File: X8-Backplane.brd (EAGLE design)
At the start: 101.9 x 101.6 mm, 17 parts

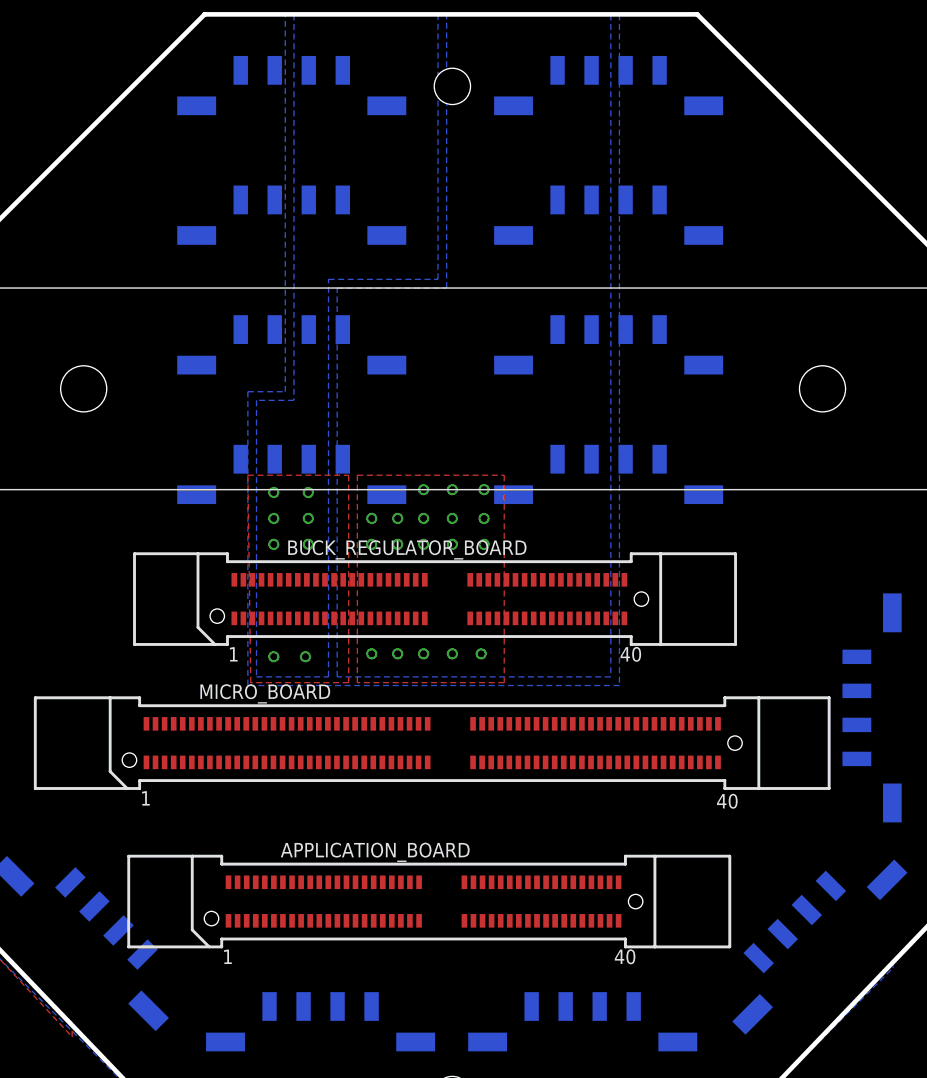
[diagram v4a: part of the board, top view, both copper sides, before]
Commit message: Routed connections from micro board
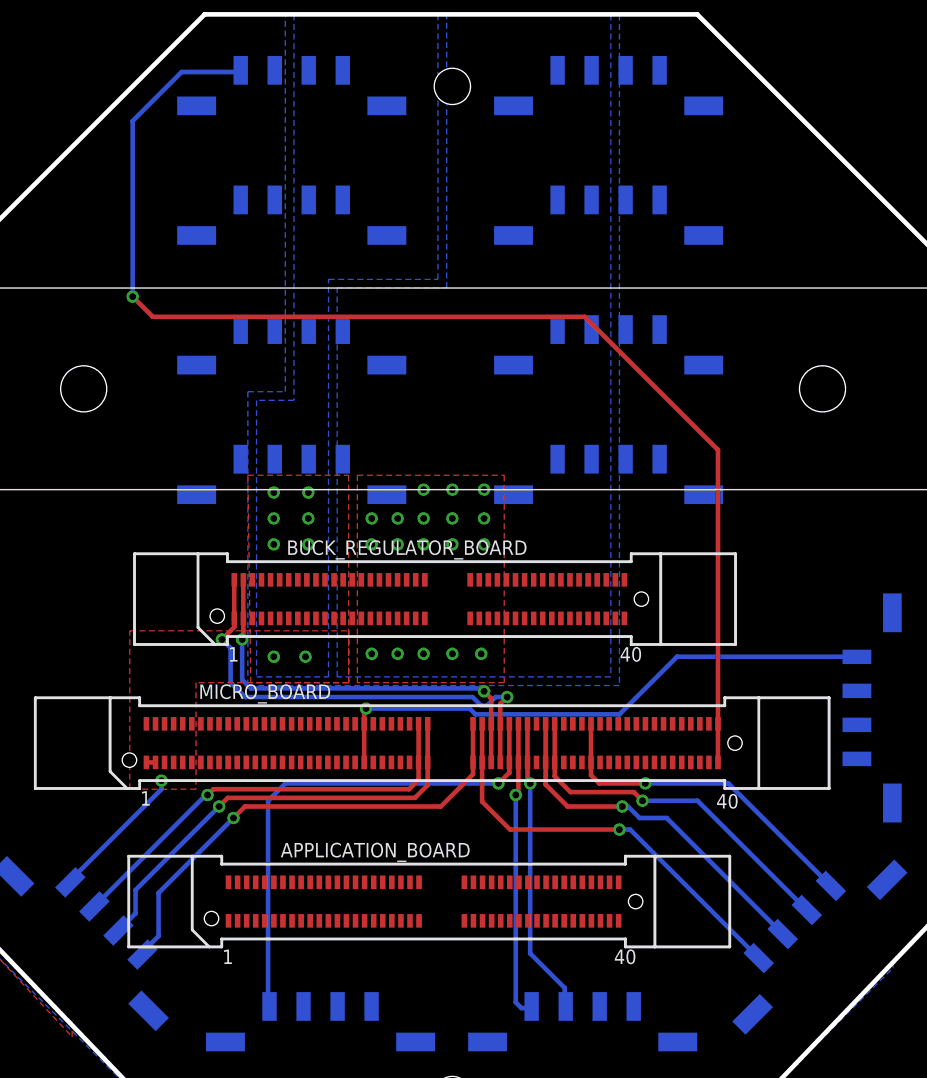
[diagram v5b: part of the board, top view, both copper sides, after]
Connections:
- removed net N$7: TEMP_SENSOR.C1
- removed net SCL: NAV_COM.C4
- removed net SDA: NAV_COM.C3
- new net BACK_UP_TEMP_DATA: MICRO_BOARD.49, MICRO_BOARD.50, TEMP_SENSOR.C1
- new net NAV_SCL: MICRO_BOARD.83, MICRO_BOARD.84, NAV_COM.C2
- new net NAV_SDA: MICRO_BOARD.81, MICRO_BOARD.82, NAV_COM.C3
- net +5V: now also MICRO_BOARD.1, MICRO_BOARD.10, MICRO_BOARD.11, MICRO_BOARD.12, MICRO_BOARD.2, MICRO_BOARD.3, MICRO_BOARD.4, MICRO_BOARD.5, MICRO_BOARD.6, MICRO_BOARD.7, MICRO_BOARD.8, MICRO_BOARD.9, SOLENOID_DATA.C4; no longer SOLENOID_DATA.C1
- net BUCK_SCL: now also MICRO_BOARD.71, MICRO_BOARD.72
- net BUCK_SDA: now also MICRO_BOARD.69, MICRO_BOARD.70
- net CANH: now also BRICKS_COM.C3, MICRO_BOARD.77, MICRO_BOARD.78; no longer BRICKS_COM.C4
- net CANL: now also BRICKS_COM.C4, MICRO_BOARD.75, MICRO_BOARD.76; no longer BRICKS_COM.C3
- net CLK: now also MICRO_BOARD.63, MICRO_BOARD.64, SOLENOID_DATA.C2; no longer SOLENOID_DATA.C3
- net DATA: now also MICRO_BOARD.65, MICRO_BOARD.66, SOLENOID_DATA.C1; no longer SOLENOID_DATA.C4
- net ENABLE: now also MICRO_BOARD.61, MICRO_BOARD.62, SOLENOID_DATA.C3; no longer SOLENOID_DATA.C2
- net GND: now also MICRO_BOARD.21, MICRO_BOARD.22, MICRO_BOARD.23, MICRO_BOARD.24, MICRO_BOARD.25, MICRO_BOARD.26, MICRO_BOARD.27, MICRO_BOARD.28, MICRO_BOARD.29, MICRO_BOARD.30, MICRO_BOARD.31, MICRO_BOARD.32, MICRO_BOARD.33, MICRO_BOARD.34, MICRO_BOARD.35, MICRO_BOARD.36
- net MAIN_SERVO: now also MICRO_BOARD.73, MICRO_BOARD.74
- net SECOND_SERVO: now also MICRO_BOARD.119, MICRO_BOARD.120
- net SONAR_DAC: now also MICRO_BOARD.91, MICRO_BOARD.92
- net SONAR_PWM: now also MICRO_BOARD.67, MICRO_BOARD.68, NAV_COM.C4; no longer NAV_COM.C2
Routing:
- net SECOND_SERVO: track 0.00 -> 111.6 mm, vias 0 -> 1
- net BACK_UP_TEMP_DATA: track 0.00 -> 50.4 mm, vias 0 -> 1
- net MAIN_SERVO: track 0.00 -> 44.8 mm, vias 0 -> 1
- net DATA: track 0.00 -> 42.5 mm, vias 0 -> 1
- net BUCK_SCL: track 0.00 -> 41.4 mm, vias 0 -> 2
- net CLK: track 0.00 -> 39.2 mm, vias 0 -> 1
- net ENABLE: track 0.00 -> 38.1 mm, vias 0 -> 1
- net BUCK_SDA: track 0.00 -> 37.1 mm, vias 0 -> 2
- net SONAR_PWM: track 0.00 -> 37.0 mm, vias 0 -> 1
- net NAV_SCL: track 0.00 -> 31.7 mm, vias 0 -> 1
- net NAV_SDA: track 0.00 -> 31.7 mm, vias 0 -> 1
- net SONAR_DAC: track 0.00 -> 29.7 mm, vias 0 -> 1
- net CANL: track 0.00 -> 26.3 mm, vias 0 -> 1
- net CANH: track 0.00 -> 26.3 mm, vias 0 -> 1
- net +5V: track 0.00 -> 13.1 mm, vias 8 -> 9

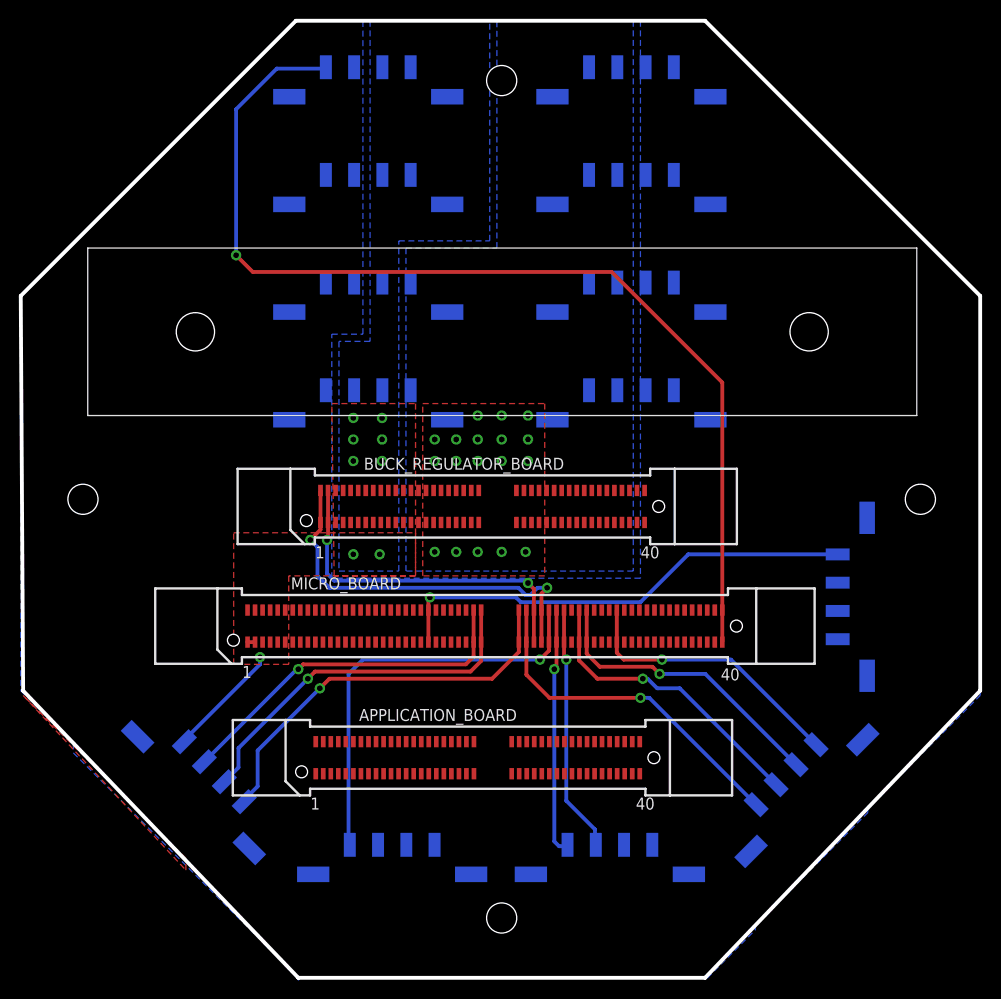
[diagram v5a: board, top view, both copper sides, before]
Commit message: Changed around the order of the connectors
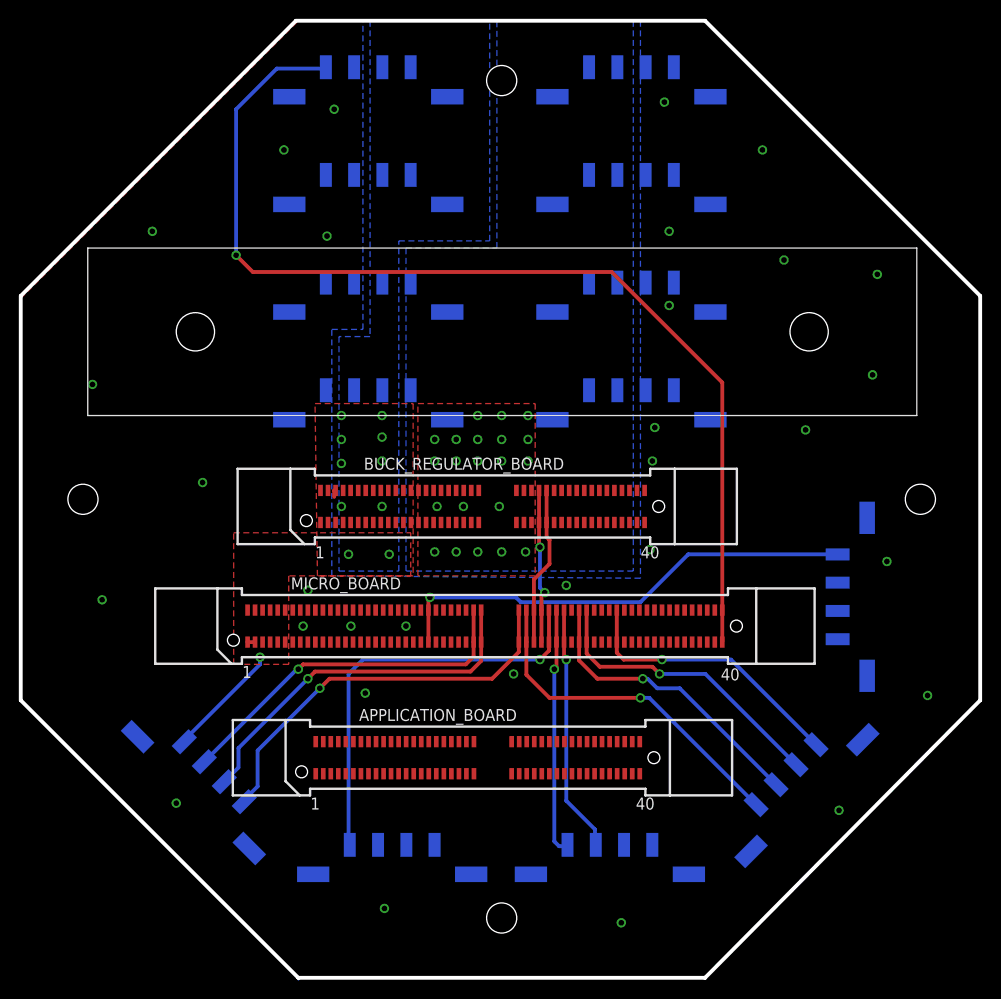
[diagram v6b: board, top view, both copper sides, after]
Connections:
- net +12V: now also BUCK_REGULATOR_BOARD.27, BUCK_REGULATOR_BOARD.28, BUCK_REGULATOR_BOARD.29, BUCK_REGULATOR_BOARD.30; no longer BUCK_REGULATOR_BOARD.51, BUCK_REGULATOR_BOARD.52
- net +5V: now also BUCK_REGULATOR_BOARD.1, BUCK_REGULATOR_BOARD.2, BUCK_REGULATOR_BOARD.3, BUCK_REGULATOR_BOARD.4
- net BUCK_SCL: now also BUCK_REGULATOR_BOARD.51, BUCK_REGULATOR_BOARD.52; no longer BUCK_REGULATOR_BOARD.1, BUCK_REGULATOR_BOARD.2
- net BUCK_SDA: now also BUCK_REGULATOR_BOARD.53, BUCK_REGULATOR_BOARD.54; no longer BUCK_REGULATOR_BOARD.3, BUCK_REGULATOR_BOARD.4
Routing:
- net BUCK_SCL: track 41.4 -> 16.5 mm
- net BUCK_SDA: track 37.1 -> 16.9 mm, vias 2 -> 0
- net +5V: track 13.1 -> 13.9 mm, vias 9 -> 11
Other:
- outline, holes or cut-outs redrawn

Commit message: Changed more connector lines
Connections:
- net BUCK_SCL: now also BUCK_REGULATOR_BOARD.53, BUCK_REGULATOR_BOARD.54; no longer BUCK_REGULATOR_BOARD.51, BUCK_REGULATOR_BOARD.52
- net BUCK_SDA: now also BUCK_REGULATOR_BOARD.51, BUCK_REGULATOR_BOARD.52; no longer BUCK_REGULATOR_BOARD.53, BUCK_REGULATOR_BOARD.54
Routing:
- net BUCK_SDA: track 16.9 -> 16.3 mm
- net BUCK_SCL: track 16.5 -> 16.4 mm, vias 2 -> 0
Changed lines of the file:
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@@
 <contactref element="MICRO_BOARD" pad="71"/>
 <wire x1="52.736" y1="37.768" x2="52.736" y2="34.368" width="0.4064" layer="1"/>
-<contactref element="BUCK_REGULATOR_BOARD" pad="52"/>
-<contactref element="BUCK_REGULATOR_BOARD" pad="51"/>
-<wire x1="52.482" y1="50.468" x2="52.482" y2="47.068" width="0.4064" layer="1"/>
-<wire x1="52.482" y1="47.068" x2="52.482" y2="44.546" width="0.4064" layer="1"/>
-<wire x1="52.482" y1="44.546" x2="52.578" y2="44.45" width="0.4064" layer="1"/>
-<via x="52.578" y="44.45" extent="1-16" drill="0.6"/>
-<wire x1="52.578" y1="44.45" x2="52.578" y2="40.132" width="0.4064" layer="16"/>
-<wire x1="52.578" y1="40.132" x2="53.086" y2="39.624" width="0.4064" layer="16"/>
-<via x="53.086" y="39.624" extent="1-16" drill="0.6"/>
-<wire x1="53.086" y1="39.624" x2="52.736" y2="39.274" width="0.4064" layer="1"/>
-<wire x1="52.736" y1="39.274" x2="52.736" y2="37.768" width="0.4064" layer="1"/>
+<contactref element="BUCK_REGULATOR_BOARD" pad="54"/>
+<contactref element="BUCK_REGULATOR_BOARD" pad="53"/>
+<wire x1="53.282" y1="50.468" x2="53.282" y2="47.068" width="0.4064" layer="1"/>
+<wire x1="52.736" y1="37.768" x2="52.736" y2="43.084" width="0.4064" layer="1"/>
+<wire x1="52.736" y1="43.084" x2="53.34" y2="43.688" width="0.4064" layer="1"/>
+<wire x1="53.282" y1="47.068" x2="53.282" y2="43.746" width="0.4064" layer="1"/>
+<wire x1="53.282" y1="43.746" x2="53.34" y2="43.688" width="0.4064" layer="1"/>
 </signal>
 <signal name="BUCK_SDA">
@@
 <contactref element="MICRO_BOARD" pad="70"/>
 <wire x1="51.936" y1="37.768" x2="51.936" y2="34.368" width="0.4064" layer="1"/>
-<contactref element="BUCK_REGULATOR_BOARD" pad="54"/>
-<contactref element="BUCK_REGULATOR_BOARD" pad="53"/>
-<wire x1="53.282" y1="50.468" x2="53.282" y2="47.068" width="0.4064" layer="1"/>
-<wire x1="53.282" y1="47.068" x2="53.282" y2="45.524" width="0.4064" layer="1"/>
-<wire x1="51.936" y1="37.768" x2="51.936" y2="41.014" width="0.4064" layer="1"/>
-<wire x1="51.936" y1="41.014" x2="53.594" y2="42.672" width="0.4064" layer="1"/>
-<wire x1="53.594" y1="42.672" x2="53.594" y2="45.212" width="0.4064" layer="1"/>
-<wire x1="53.594" y1="45.212" x2="53.282" y2="45.524" width="0.4064" layer="1"/>
+<contactref element="BUCK_REGULATOR_BOARD" pad="52"/>
+<contactref element="BUCK_REGULATOR_BOARD" pad="51"/>
+<wire x1="52.482" y1="50.468" x2="52.482" y2="47.068" width="0.4064" layer="1"/>
+<wire x1="51.936" y1="37.768" x2="51.936" y2="43.3" width="0.4064" layer="1"/>
+<wire x1="51.936" y1="43.3" x2="52.482" y2="43.846" width="0.4064" layer="1"/>
+<wire x1="52.482" y1="47.068" x2="52.482" y2="43.846" width="0.4064" layer="1"/>
 </signal>
 <signal name="SECOND_SERVO">

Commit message: Finished the backplane
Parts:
- removed MA5N_CAM_POW: MICRO-FIT-4-SMD-PART, Connectors:MICRO-FIT-4-SMD
- added MAIN_CAM_POW: MICRO-FIT-4-SMD-PART, Connectors:MICRO-FIT-4-SMD
- moved POWER_INPUT 143.1 mm to (-2.54, -53.3)
- moved SOLENOID_POWER 123.8 mm to (-2.54, -41.4)
- moved EXTRA_SERVO 120.9 mm to (43.2, -29.5)
- moved TEMP_SENSOR 113.2 mm to (20.3, -41.4), turned to 0 degrees
- moved BUCK_REGULATOR_BOARD 106.1 mm to (-0.25, -46.5), turned to 180 degrees
- moved NAV_COM 95.6 mm to (-2.54, 53.3), turned to 0 degrees
- moved SEC_CAM_2 90.4 mm to (-2.54, 29.5)
- moved SEC_CAM_1 90.1 mm to (-2.54, 41.4)
- moved MICRO_BOARD 79.8 mm to (-1.27, -27.7), turned to 180 degrees
- moved BRICKS_COM 79.7 mm to (20.3, -53.3)
- moved APPLICATION_BOARD 53.6 mm to (-5.59, 7.37), turned to 180 degrees
- moved U$18 46.1 mm to (44.5, 35.3), turned to 180 degrees
- moved SOLENOID_DATA 40.2 mm to (20.3, -29.5), turned to 0 degrees
- moved ETH_POWER 37.3 mm to (36.1, 43.7), flipped to the top, turned to 135 degrees
- moved MAIN_CAM_DATA 33.7 mm to (20.3, 29.5)
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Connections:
- net +12V: now also APPLICATION_BOARD.21, APPLICATION_BOARD.22, APPLICATION_BOARD.23, APPLICATION_BOARD.24, APPLICATION_BOARD.25, APPLICATION_BOARD.26, APPLICATION_BOARD.27, APPLICATION_BOARD.28, APPLICATION_BOARD.29, APPLICATION_BOARD.30, APPLICATION_BOARD.31, APPLICATION_BOARD.32, APPLICATION_BOARD.33, APPLICATION_BOARD.34, MAIN_CAM_POW.C4, NAV_POWER.C4, POWER_INPUT.C1, POWER_INPUT.C2, SEC_CAM_1.C1, SEC_CAM_1.C2, SEC_CAM_2.C1, SEC_CAM_2.C2, SOLENOID_POWER.C1, SOLENOID_POWER.C2; no longer MA5N_CAM_POW.C1, NAV_POWER.C1, POWER_INPUT.C3, POWER_INPUT.C4, SEC_CAM_1.C3, SEC_CAM_1.C4, SEC_CAM_2.C3, SEC_CAM_2.C4, SOLENOID_POWER.C3, SOLENOID_POWER.C4
- net +3V3: now also APPLICATION_BOARD.57, APPLICATION_BOARD.58
- net +5V: now also APPLICATION_BOARD.10, APPLICATION_BOARD.11, APPLICATION_BOARD.12, APPLICATION_BOARD.13, APPLICATION_BOARD.14, APPLICATION_BOARD.15, APPLICATION_BOARD.16, APPLICATION_BOARD.17, APPLICATION_BOARD.18, APPLICATION_BOARD.19, APPLICATION_BOARD.20, APPLICATION_BOARD.9, EXTRA_SERVO.C4, MAIN_CAM_DATA.C1, MAIN_CAM_DATA.C2, NAV_POWER.C1, SOLENOID_DATA.C1; no longer EXTRA_SERVO.C2, MA5N_CAM_POW.C2, MA5N_CAM_POW.C3, NAV_POWER.C2, SOLENOID_DATA.C4
- net CANH: now also APPLICATION_BOARD.69, APPLICATION_BOARD.70, BRICKS_COM.C4; no longer BRICKS_COM.C3
- net CANL: now also APPLICATION_BOARD.65, APPLICATION_BOARD.66, BRICKS_COM.C3; no longer BRICKS_COM.C4
- net CLK: now also SOLENOID_DATA.C3; no longer SOLENOID_DATA.C2
- net DATA: now also SOLENOID_DATA.C4; no longer SOLENOID_DATA.C1
- net ENABLE: now also SOLENOID_DATA.C2; no longer SOLENOID_DATA.C3
- net GND: now also APPLICATION_BOARD.37, APPLICATION_BOARD.38, APPLICATION_BOARD.39, APPLICATION_BOARD.40, APPLICATION_BOARD.41, APPLICATION_BOARD.42, APPLICATION_BOARD.43, APPLICATION_BOARD.44, APPLICATION_BOARD.45, APPLICATION_BOARD.46, APPLICATION_BOARD.47, APPLICATION_BOARD.48, APPLICATION_BOARD.49, APPLICATION_BOARD.50, APPLICATION_BOARD.51, APPLICATION_BOARD.52, MAIN_CAM_POW.C1, MAIN_CAM_POW.C2, MAIN_CAM_POW.C3, NAV_POWER.C2, POWER_INPUT.C3, POWER_INPUT.C4, SEC_CAM_1.C3, SEC_CAM_1.C4, SEC_CAM_2.C3, SEC_CAM_2.C4, SOLENOID_POWER.C3, SOLENOID_POWER.C4; no longer MA5N_CAM_POW.C4, MAIN_CAM_DATA.C1, MAIN_CAM_DATA.C2, NAV_POWER.C4, POWER_INPUT.C1, POWER_INPUT.C2, SEC_CAM_1.C1, SEC_CAM_1.C2, SEC_CAM_2.C1, SEC_CAM_2.C2, SOLENOID_POWER.C1, SOLENOID_POWER.C2
- net LED_PWM: now also APPLICATION_BOARD.1, APPLICATION_BOARD.2, APPLICATION_BOARD.3, APPLICATION_BOARD.4, APPLICATION_BOARD.5, APPLICATION_BOARD.6, APPLICATION_BOARD.7, APPLICATION_BOARD.8
- net SECOND_SERVO: now also EXTRA_SERVO.C2; no longer EXTRA_SERVO.C4
- net TEMP_DATA: now also APPLICATION_BOARD.59, APPLICATION_BOARD.60
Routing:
- net TEMP_DATA: track 0.00 -> 107.1 mm, vias 0 -> 1
- net +3V3: track 0.00 -> 105.7 mm, vias 0 -> 1
- net SONAR_DAC: track 29.7 -> 124.4 mm
- net NAV_SCL: track 31.7 -> 120.8 mm
- net NAV_SDA: track 31.7 -> 114.7 mm
- net SONAR_PWM: track 37.0 -> 114.4 mm
- net CANH: track 26.3 -> 75.3 mm, vias 1 -> 3
- net CANL: track 26.3 -> 75.1 mm, vias 1 -> 3
- net BACK_UP_TEMP_DATA: track 50.4 -> 18.4 mm
- net MAIN_SERVO: track 44.8 -> 73.3 mm, vias 1 -> 3
- net DATA: track 42.5 -> 20.7 mm
- net CLK: track 39.2 -> 19.3 mm
- net ENABLE: track 38.1 -> 19.7 mm
- net SECOND_SERVO: track 111.6 -> 125.0 mm
- net BUCK_SDA: track 16.3 -> 22.3 mm
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- added copper zone on layer 1, net LED_PWM
- added copper zone on layer 16, net LED_PWM
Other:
- board size 101.9 x 101.6 mm -> 122.1 x 122.1 mm
